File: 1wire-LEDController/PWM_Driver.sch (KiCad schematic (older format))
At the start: 13 parts, among them CON1 BARREL_JACK, P3 CONN_01X05, P4 DC_IN, P5 CONN_01X05, Q1 IRLZ44NS, Q2 IRLZ44NS, Q3 IRLZ44NS, Q4 IRLZ44NS, Q5 IRLZ44NS, Q6 IRLZ44NS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

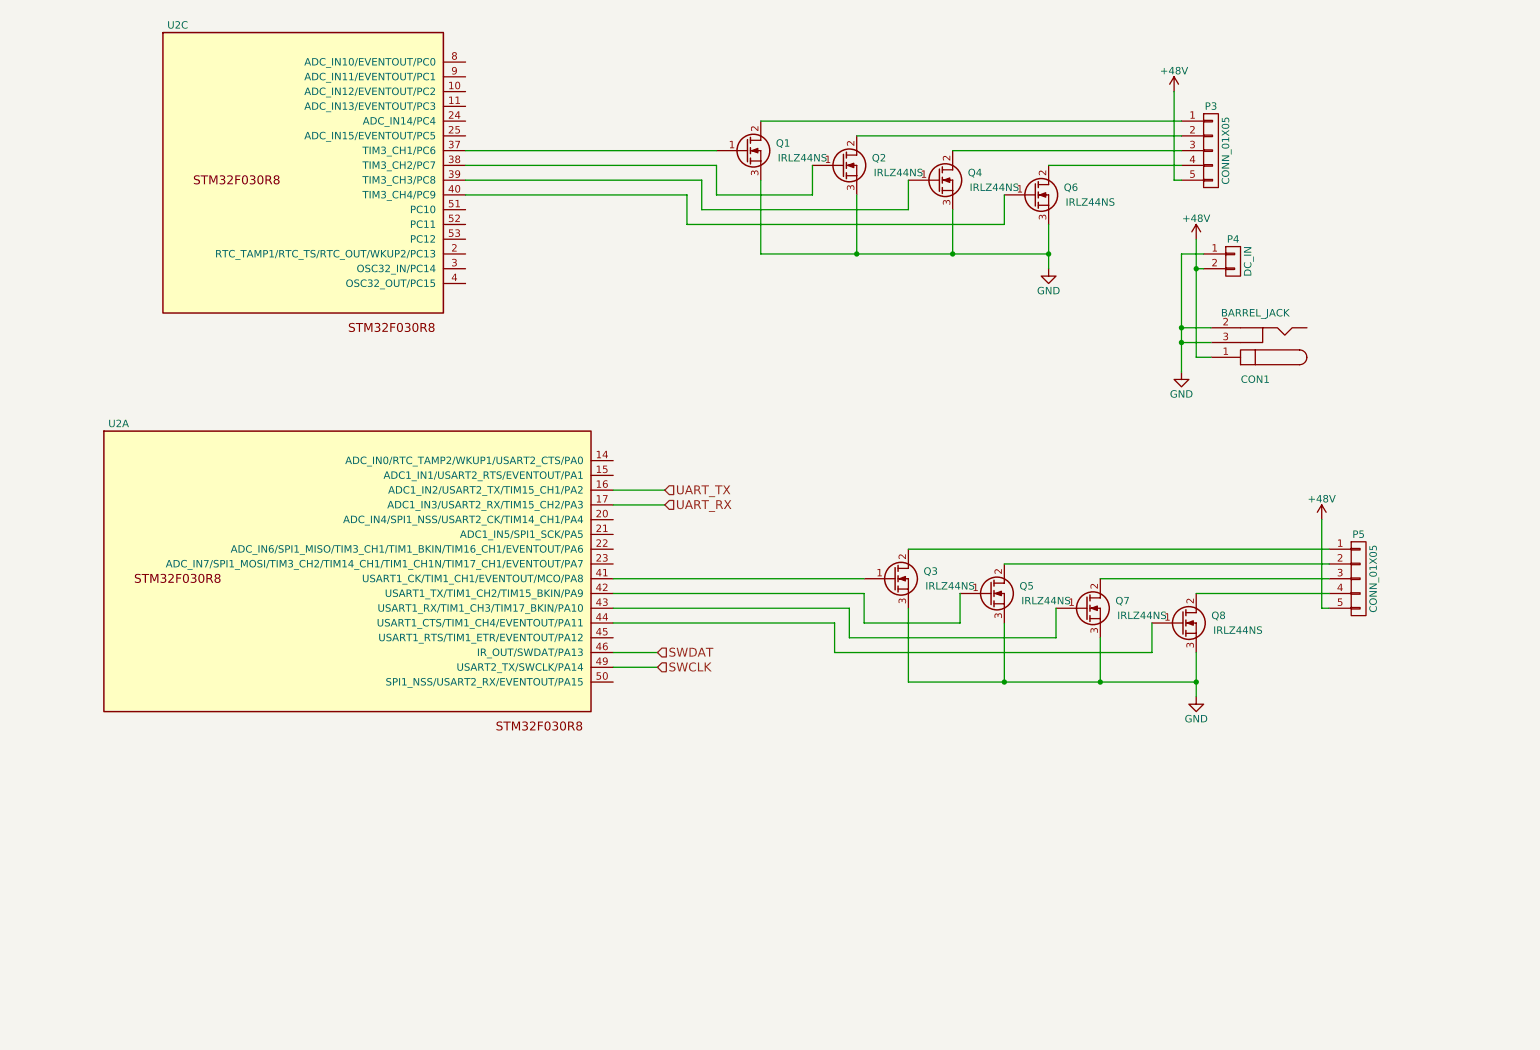
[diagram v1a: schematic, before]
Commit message: Add 4 channel RGBW LED controller
Signed-off-by: Alastair D'Silva <alastair@d-silva.org>
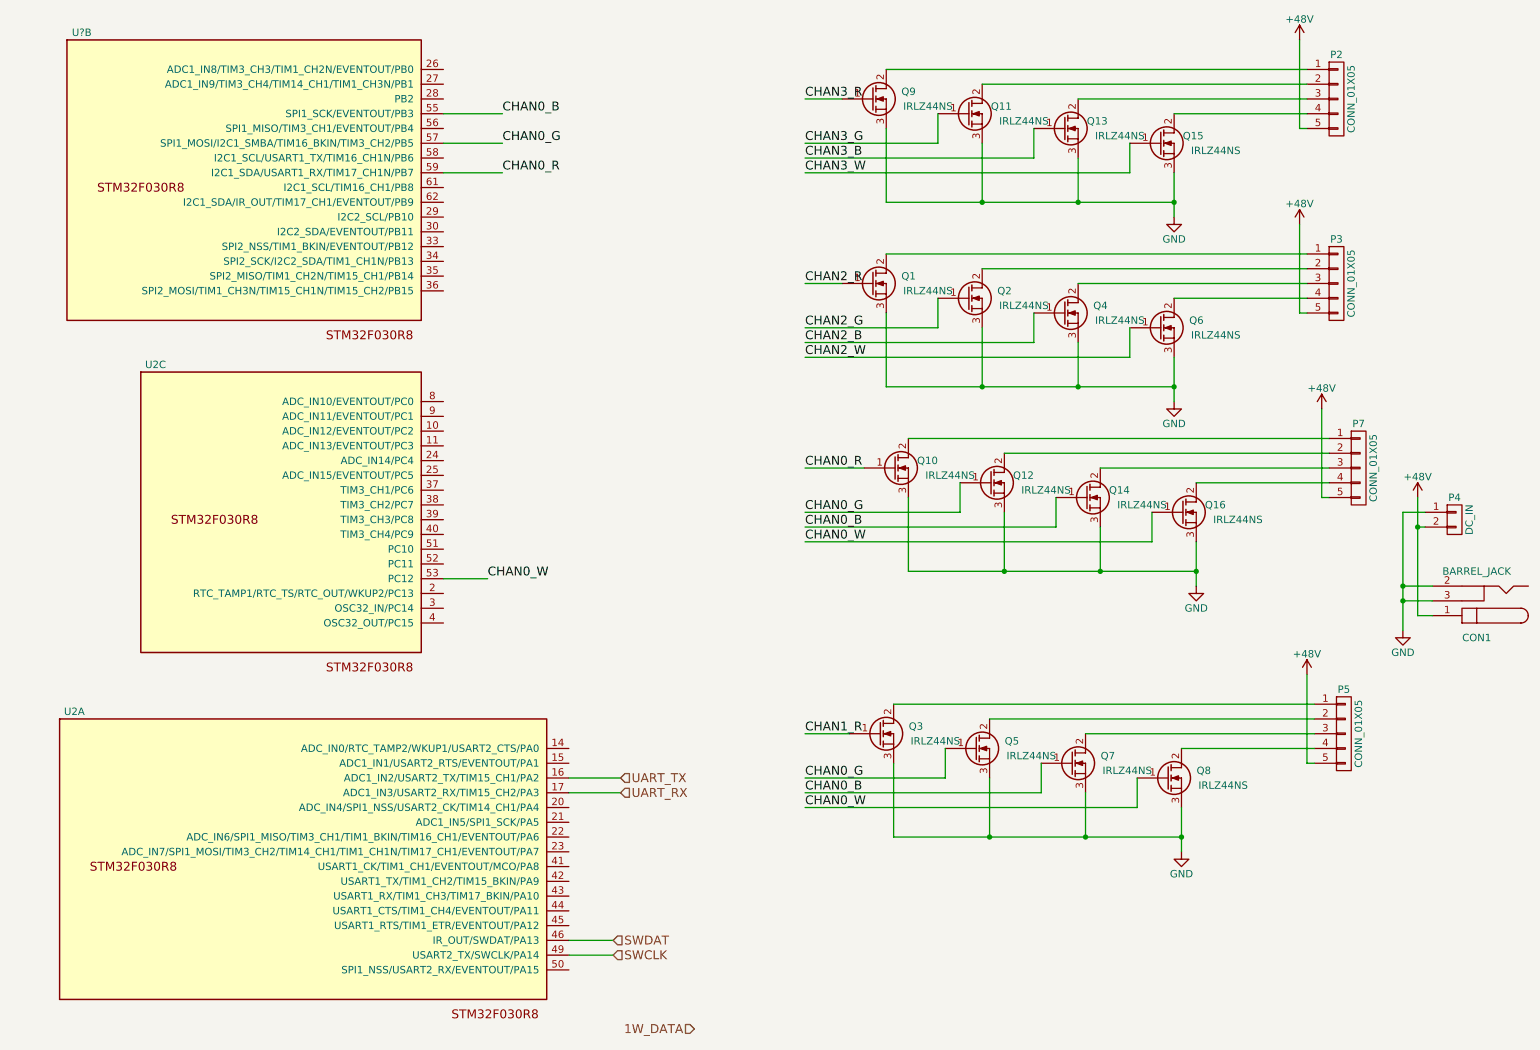
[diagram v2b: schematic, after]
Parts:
- added P2, P7: CONN_01X05, 2EDCK-Screw-Connectors:2EDCK-5.08-5PIN, symbol CONN_01X05
- added Q10, Q11, Q12, Q13, Q14, Q15, Q16, Q9: IRLZ44NS, kicad-open-modules:D2PAK, symbol Q_NMOS_GDS
- added U?: STM32F030R8, LQFP-64, symbol STM32F030R8
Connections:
- net +48V: now also P2.5 (P5), P7.5 (P5)
- net GND: now also Q10.3 (S), Q11.3 (S), Q12.3 (S), Q13.3 (S), Q14.3 (S), Q15.3 (S), Q16.3 (S), Q9.3 (S)
- net at U2.37 (TIM3_CH1/PC6): no longer Q1.1 (G)
- net at U2.38 (TIM3_CH2/PC7): no longer Q2.1 (G)
- net at U2.39 (TIM3_CH3/PC8): no longer Q4.1 (G)
- net at U2.40 (TIM3_CH4/PC9): no longer Q6.1 (G)
- net CHAN0_W: now reaches U2.53 (PC12)
- net CHAN0_W: now also Q8.1 (G), Q16.1 (G)
- net at U2.41 (USART1_CK/TIM1_CH1/EVENTOUT/MCO/PA8): no longer Q3.1 (G)
- net at U2.42 (USART1_TX/TIM1_CH2/TIM15_BKIN/PA9): no longer Q5.1 (G)
- net at U2.43 (USART1_RX/TIM1_CH3/TIM17_BKIN/PA10): no longer Q7.1 (G)
- net at U2.44 (USART1_CTS/TIM1_CH4/EVENTOUT/PA11): no longer Q8.1 (G)
- new net: P7.1 (P1), Q10.2 (D)
- new net: P7.2 (P2), Q12.2 (D)
- new net: P7.3 (P3), Q14.2 (D)
- new net: P7.4 (P4), Q16.2 (D)
- new net: P2.1 (P1), Q9.2 (D)
- new net: P2.2 (P2), Q11.2 (D)
- new net: P2.3 (P3), Q13.2 (D)
- new net: P2.4 (P4), Q15.2 (D)
- new net CHAN0_B: Q14.1 (G), Q7.1 (G), U?.55 (SPI1_SCK/EVENTOUT/PB3)
- new net CHAN0_G: Q12.1 (G), Q5.1 (G), U?.57 (SPI1_MOSI/I2C1_SMBA/TIM16_BKIN/TIM3_CH2/PB5)
- new net CHAN0_R: Q10.1 (G), U?.59 (I2C1_SDA/USART1_RX/TIM17_CH1N/PB7)
- new net CHAN1_R: Q3.1 (G)
- new net CHAN2_B: Q4.1 (G)
- new net CHAN2_G: Q2.1 (G)
- new net CHAN2_R: Q1.1 (G)
- new net CHAN2_W: Q6.1 (G)
- new net CHAN3_B: Q13.1 (G)
- new net CHAN3_G: Q11.1 (G)
- new net CHAN3_R: Q9.1 (G)
- new net CHAN3_W: Q15.1 (G)
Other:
- moved on the sheet: CON1, P3, P4, P5, Q1, Q2, Q3, Q4, Q5, Q6, Q7, Q8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
